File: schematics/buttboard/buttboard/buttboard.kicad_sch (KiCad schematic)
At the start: 11 parts, among them J1 Conn_01x05

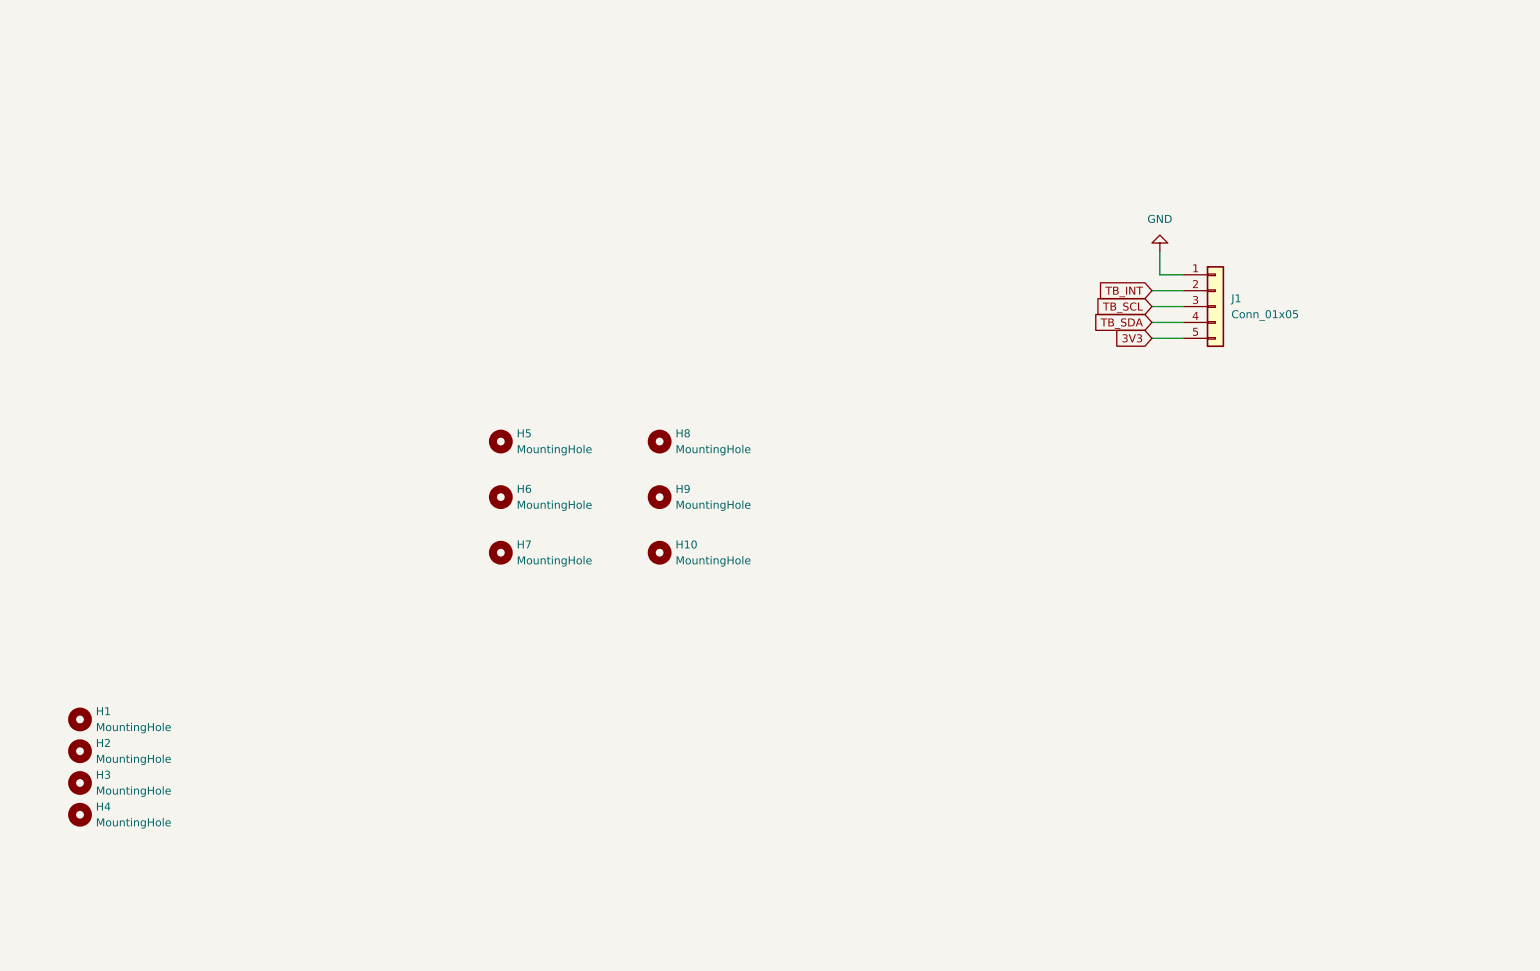
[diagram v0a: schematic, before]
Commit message: Added membrane button footprint to buttboard.
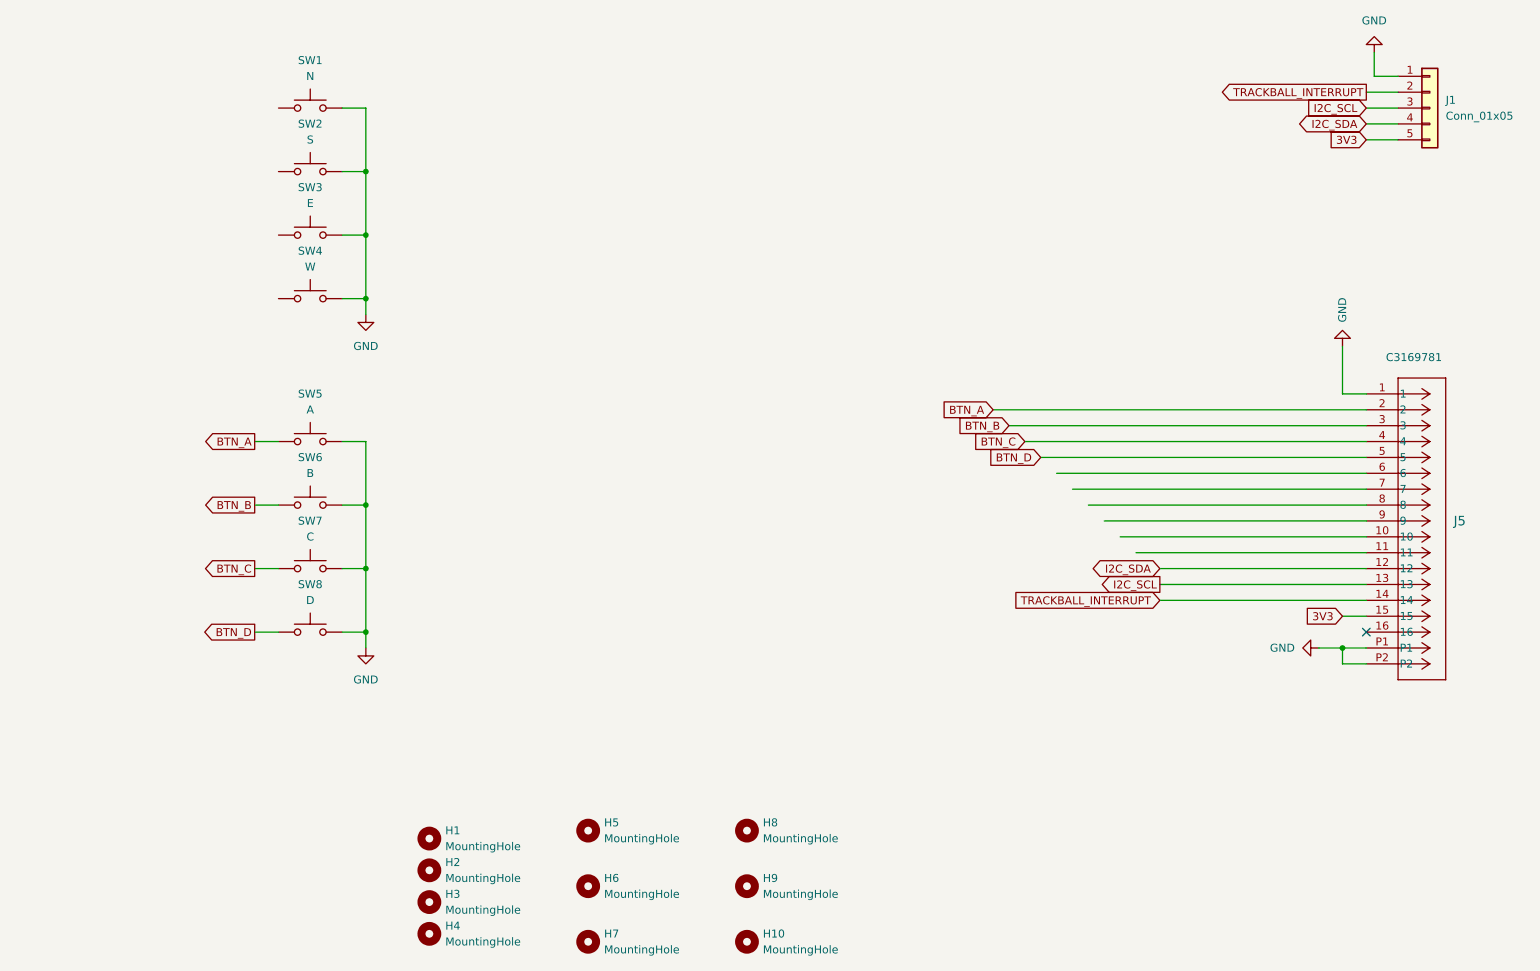
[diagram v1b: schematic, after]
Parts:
- added J5: 527461671, CON_527461671_MOL, symbol CON_527461671_MOL:527461671
- added SW1: N, MEMBRANE:MEMBRANE_A, symbol Switch:SW_Push
- added SW2: S, MEMBRANE:MEMBRANE_A, symbol Switch:SW_Push
- added SW3: E, MEMBRANE:MEMBRANE_A, symbol Switch:SW_Push
- added SW4: W, MEMBRANE:MEMBRANE_A, symbol Switch:SW_Push
- added SW5: A, MEMBRANE:MEMBRANE_A, symbol Switch:SW_Push
- added SW6: B, MEMBRANE:MEMBRANE_A, symbol Switch:SW_Push
- added SW7: C, MEMBRANE:MEMBRANE_A, symbol Switch:SW_Push
- added SW8: D, MEMBRANE:MEMBRANE_A, symbol Switch:SW_Push
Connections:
- net 3V3: now also J5.15
- net GND: now also J5.1, J5.P1, J5.P2, SW1.2, SW2.2, SW3.2, SW4.2, SW5.2, SW6.2, SW7.2, SW8.2
- net TB_INT renamed TRACKBALL_INTERRUPT
- net TRACKBALL_INTERRUPT: now also J5.14
- net TB_SCL renamed I2C_SCL
- net I2C_SCL: now also J5.13
- net TB_SDA renamed I2C_SDA
- net I2C_SDA: now also J5.12
- new net BTN_A: J5.2, SW5.1
- new net BTN_B: J5.3, SW6.1
- new net BTN_C: J5.4, SW7.1
- new net BTN_D: J5.5, SW8.1
- no-connect marks 0 -> 1
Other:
- moved on the sheet: H1, H10, H2, H3, H4, H5, H6, H7, H8, H9, J1

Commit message: Replaced membrane buttons with tactile buttons on buttboard.
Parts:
- SW1, SW2, SW3, SW4, SW5, SW6, SW7, SW8: footprint MEMBRANE:MEMBRANE_A -> Button_Switch_THT:SW_PUSH_6mm_H7.3mm
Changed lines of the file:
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@@
 			)
 		)
-		(property "Footprint" "MEMBRANE:MEMBRANE_A"
+		(property "Footprint" "Button_Switch_THT:SW_PUSH_6mm_H7.3mm"
 			(at 81.28 114.3 0)
 			(effects
@@
 			)
 		)
-		(property "Footprint" "MEMBRANE:MEMBRANE_A"
+		(property "Footprint" "Button_Switch_THT:SW_PUSH_6mm_H7.3mm"
 			(at 81.28 134.62 0)
 			(effects
@@
 			)
 		)
-		(property "Footprint" "MEMBRANE:MEMBRANE_A"
+		(property "Footprint" "Button_Switch_THT:SW_PUSH_6mm_H7.3mm"
 			(at 81.28 71.12 0)
 			(effects
@@
 			)
 		)
-		(property "Footprint" "MEMBRANE:MEMBRANE_A"
+		(property "Footprint" "Button_Switch_THT:SW_PUSH_6mm_H7.3mm"
 			(at 81.28 50.8 0)
 			(effects
@@
 			)
 		)
-		(property "Footprint" "MEMBRANE:MEMBRANE_A"
+		(property "Footprint" "Button_Switch_THT:SW_PUSH_6mm_H7.3mm"
 			(at 81.28 124.46 0)
 			(effects
@@
 			)
 		)
-		(property "Footprint" "MEMBRANE:MEMBRANE_A"
+		(property "Footprint" "Button_Switch_THT:SW_PUSH_6mm_H7.3mm"
 			(at 81.28 60.96 0)
 			(effects
@@
 			)
 		)
-		(property "Footprint" "MEMBRANE:MEMBRANE_A"
+		(property "Footprint" "Button_Switch_THT:SW_PUSH_6mm_H7.3mm"
 			(at 81.28 81.28 0)
 			(effects
@@
 			)
 		)
-		(property "Footprint" "MEMBRANE:MEMBRANE_A"
+		(property "Footprint" "Button_Switch_THT:SW_PUSH_6mm_H7.3mm"
 			(at 81.28 104.14 0)
 			(effects

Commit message: More work on buttboard.
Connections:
- net BTN_DPAD_E: now reaches SW3.1
- net BTN_DPAD_E: now also J5.8
- net BTN_DPAD_N: now reaches J5.6
- net BTN_DPAD_N: now also SW1.1
- net BTN_DPAD_S: now reaches J5.7
- net BTN_DPAD_S: now also SW2.1
- net BTN_DPAD_W: now reaches J5.9
- net BTN_DPAD_W: now also SW4.1
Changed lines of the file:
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@@
+	(wire
+		(pts
+			(xy 71.12 76.2) (xy 76.2 76.2)
+		)
+		(stroke
+			(width 0)
+			(type default)
+		)
+	)
 	(wire
 		(pts
@@
 	(wire
 		(pts
+			(xy 71.12 66.04) (xy 76.2 66.04)
+		)
+		(stroke
+			(width 0)
+			(type default)
+		)
+	)
+	(wire
+		(pts
 			(xy 200.66 114.3) (xy 250.19 114.3)
 		)
@@
 	(wire
 		(pts
+			(xy 71.12 55.88) (xy 76.2 55.88)
+		)
+		(stroke
+			(width 0)
+			(type default)
+		)
+	)
+	(wire
+		(pts
 			(xy 90.17 139.7) (xy 90.17 142.24)
 		)
@@
 	(wire
 		(pts
+			(xy 71.12 86.36) (xy 76.2 86.36)
+		)
+		(stroke
+			(width 0)
+			(type default)
+		)
+	)
+	(wire
+		(pts
 			(xy 195.58 109.22) (xy 250.19 109.22)
 		)
@@
 			(width 0)
 			(type default)
+		)
+	)
+	(global_label "BTN_DPAD_W"
+		(shape output)
+		(at 71.12 86.36 180)
+		(fields_autoplaced yes)
+		(effects
+			(font
+				(size 1.27 1.27)
+			)
+			(justify right)
+		)
+		(property "Intersheetrefs" "${INTERSHEET_REFS}"
+			(at 56.2815 86.36 0)
+			(effects
+				(font
+					(size 1.27 1.27)
+				)
+				(justify right)
+				(hide yes)
+			)
 		)
 	)
@@
 		)
 	)
+	(global_label "BTN_DPAD_S"
+		(shape output)
+		(at 71.12 66.04 180)
+		(fields_autoplaced yes)
+		(effects
+			(font
+				(size 1.27 1.27)
+			)
+			(justify right)
+		)
+		(property "Intersheetrefs" "${INTERSHEET_REFS}"
+			(at 56.5234 66.04 0)
+			(effects
+				(font
+					(size 1.27 1.27)
+				)
+				(justify right)
+				(hide yes)
+			)
+		)
+	)
 	(global_label "BTN_B"
 		(shape output)
@@
 		)
 	)
+	(global_label "BTN_DPAD_W"
+		(shape input)
+		(at 208.28 121.92 180)
+		(fields_autoplaced yes)
+		(effects
+			(font
+				(size 1.27 1.27)
+			)
+			(justify right)
+		)
+		(property "Intersheetrefs" "${INTERSHEET_REFS}"
+			(at 193.4415 121.92 0)
+			(effects
+				(font
+					(size 1.27 1.27)
+				)
+				(justify right)
+				(hide yes)
+			)
+		)
+	)
 	(global_label "BTN_D"
 		(shape input)
@@
 		)
 	)
+	(global_label "BTN_DPAD_S"
+		(shape input)
+		(at 203.2 116.84 180)
+		(fields_autoplaced yes)
+		(effects
+			(font
+				(size 1.27 1.27)
+			)
+			(justify right)
+		)
+		(property "Intersheetrefs" "${INTERSHEET_REFS}"
+			(at 188.6034 116.84 0)
+			(effects
+				(font
+					(size 1.27 1.27)
+				)
+				(justify right)
+				(hide yes)
+			)
+		)
+	)
 	(global_label "BTN_A"
 		(shape output)
@@
 		)
 	)
+	(global_label "BTN_DPAD_N"
+		(shape input)
+		(at 200.66 114.3 180)
+		(fields_autoplaced yes)
+		(effects
+			(font
+				(size 1.27 1.27)
+			)
+			(justify right)
+		)
+		(property "Intersheetrefs" "${INTERSHEET_REFS}"
+			(at 185.9424 114.3 0)
+			(effects
+				(font
+					(size 1.27 1.27)
+				)
+				(justify right)
+				(hide yes)
+			)
+		)
+	)
 	(global_label "BTN_C"
 		(shape input)
@@
 		(property "Intersheetrefs" "${INTERSHEET_REFS}"
 			(at 243.6972 60.96 0)
+			(effects
+				(font
+					(size 1.27 1.27)
+				)
+				(justify right)
+				(hide yes)
+			)
+		)
+	)
+	(global_label "BTN_DPAD_E"
+		(shape output)
+		(at 71.12 76.2 180)
+		(fields_autoplaced yes)
+		(effects
+			(font
+				(size 1.27 1.27)
+			)
+			(justify right)
+		)
+		(property "Intersheetrefs" "${INTERSHEET_REFS}"
+			(at 56.5839 76.2 0)
+			(effects
+				(font
+					(size 1.27 1.27)
+				)
+				(justify right)
+				(hide yes)
+			)
+		)
+	)
+	(global_label "BTN_DPAD_E"
+		(shape input)
+		(at 205.74 119.38 180)
+		(fields_autoplaced yes)
+		(effects
+			(font
+				(size 1.27 1.27)
+			)
+			(justify right)
+		)
+		(property "Intersheetrefs" "${INTERSHEET_REFS}"
+			(at 191.2039 119.38 0)
 			(effects
 				(font
@@
 			(effects
 				(font
+					(size 1.27 1.27)
+				)
+				(justify right)
+				(hide yes)
+			)
+		)
+	)
+	(global_label "BTN_DPAD_N"
+		(shape output)
+		(at 71.12 55.88 180)
+		(fields_autoplaced yes)
+		(effects
+			(font
+				(size 1.27 1.27)
+			)
+			(justify right)
+		)
+		(property "Intersheetrefs" "${INTERSHEET_REFS}"
+			(at 56.4024 55.88 0)
+			(effects
+				(font

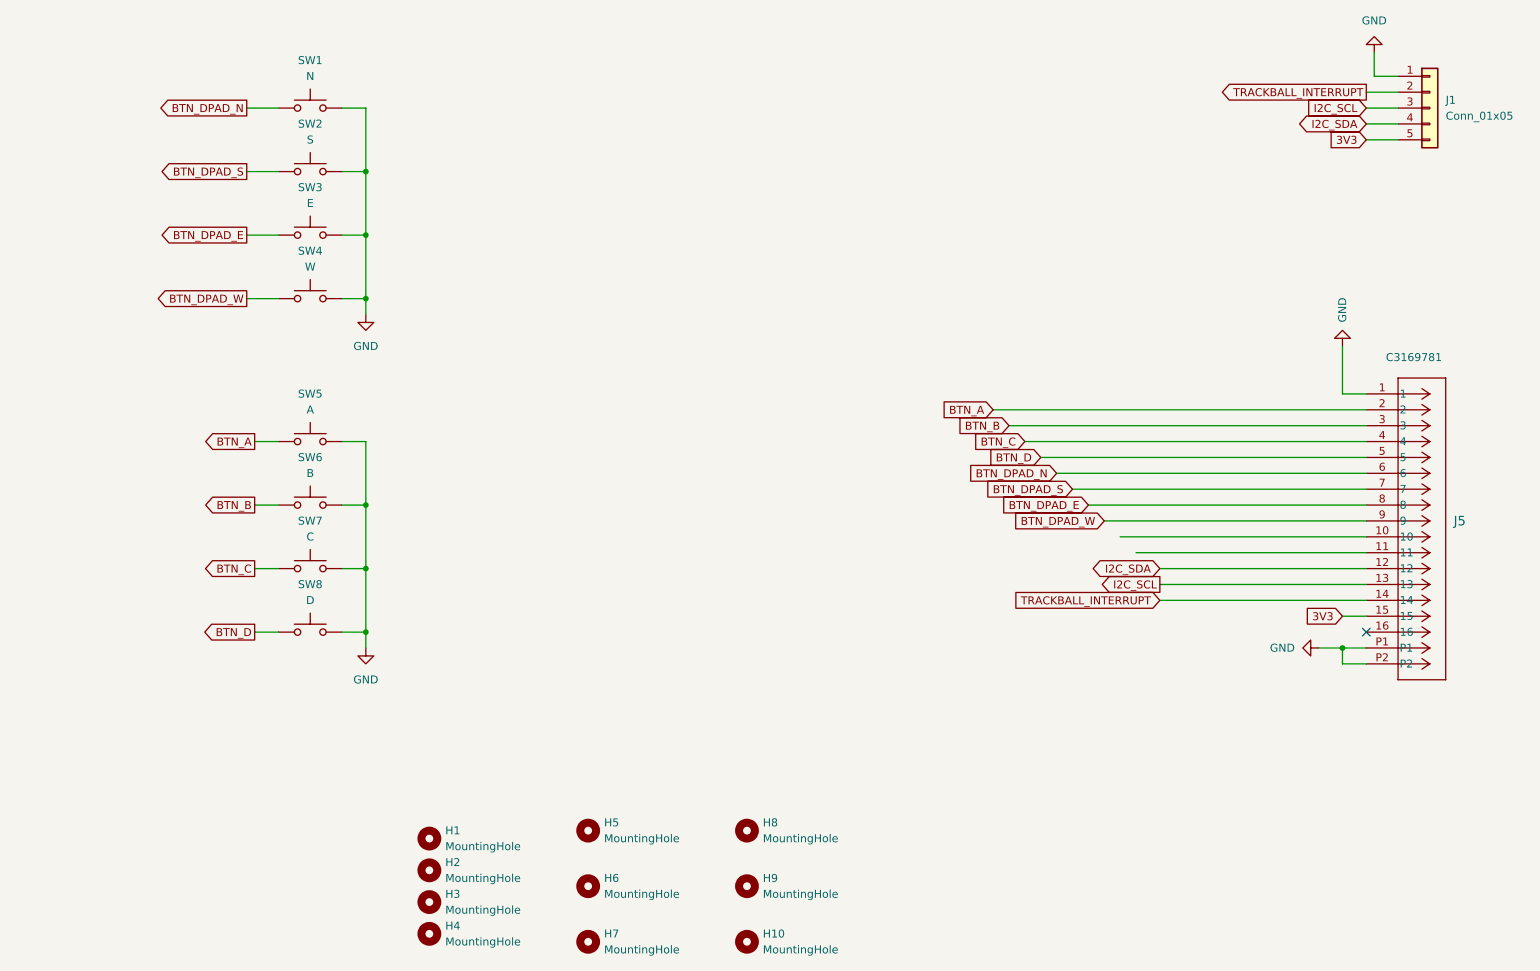
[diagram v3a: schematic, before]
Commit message: Added control buttons to buttboard; adjusted cutout.
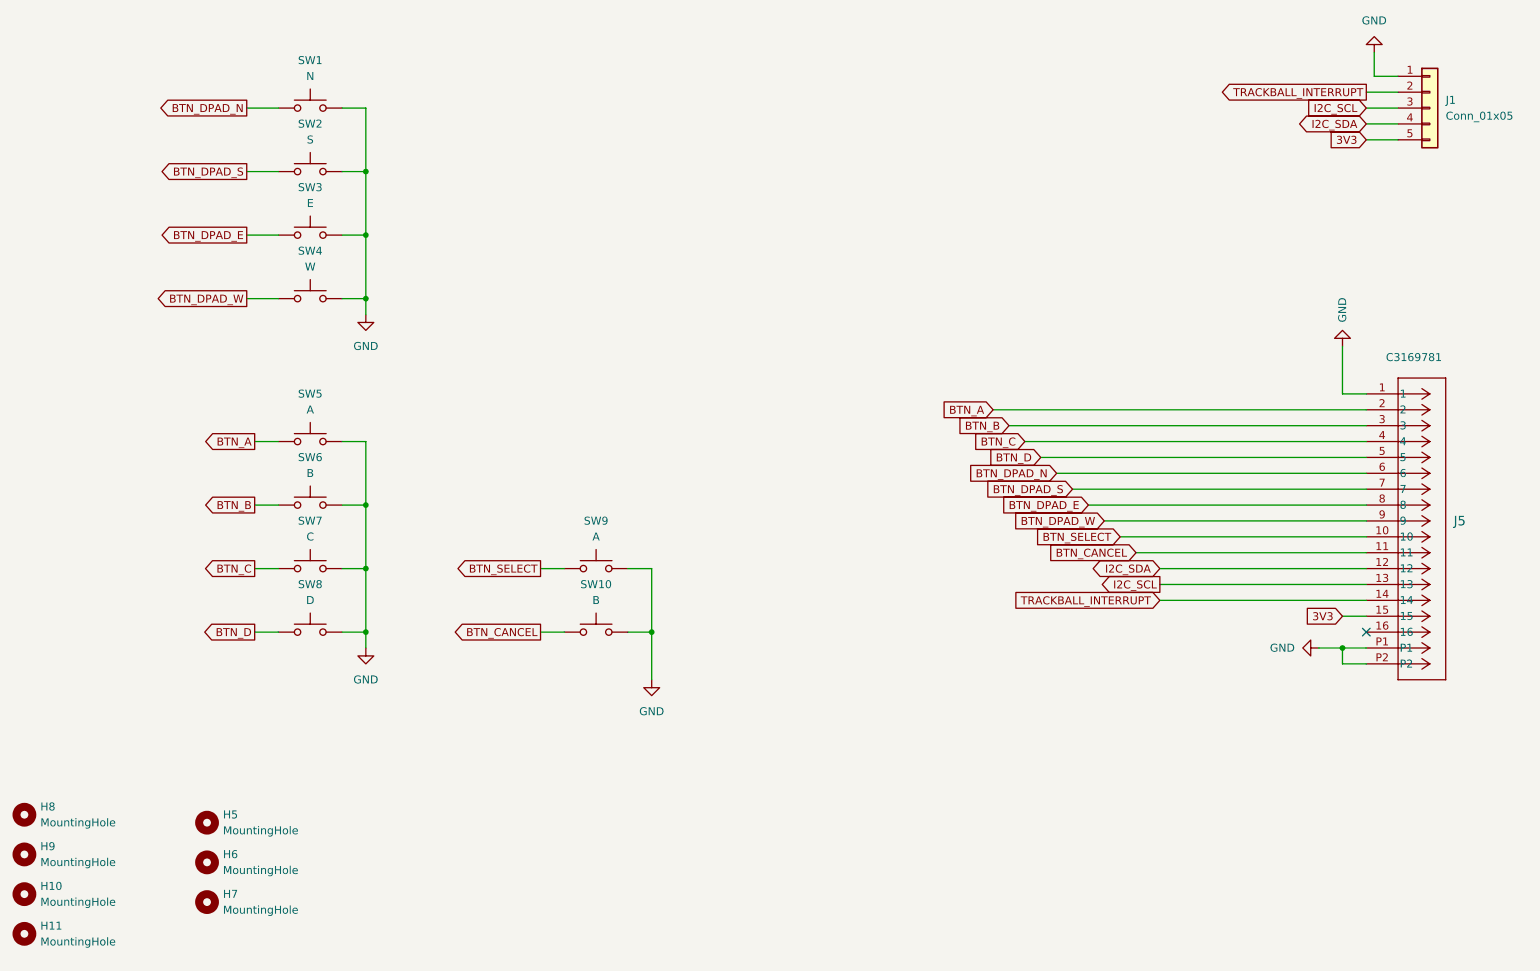
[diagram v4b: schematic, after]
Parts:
- removed H1, H2, H3, H4: MountingHole, MountingHole:MountingHole_2.2mm_M2, symbol Mechanical:MountingHole
- added H11: MountingHole, MountingHole:MountingHole_3mm, symbol Mechanical:MountingHole
- added SW10: B, Button_Switch_THT:SW_PUSH_6mm_H7.3mm, symbol Switch:SW_Push
- added SW9: A, Button_Switch_THT:SW_PUSH_6mm_H7.3mm, symbol Switch:SW_Push
- H10, H5, H6, H7, H8, H9: footprint MountingHole:MountingHole_2.5mm -> MountingHole:MountingHole_3mm
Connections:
- net GND: now also SW10.2, SW9.2
- net BTN_SELECT: now reaches J5.10
- net BTN_SELECT: now also SW9.1
- net BTN_CANCEL: now reaches J5.11
- net BTN_CANCEL: now also SW10.1
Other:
- moved on the sheet: H10, H5, H6, H7, H8, H9
